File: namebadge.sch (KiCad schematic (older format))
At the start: 2 parts, among them U1 Pico

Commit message: power cap
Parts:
- added C15: 1000uF, Capacitor_THT:C_Radial_D12.5mm_H20.0mm_P5.00mm, symbol Device:C
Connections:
- net labels removed: Neo_DIN
- wire segments 22 -> 28
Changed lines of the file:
@@
 	1    0    0    -1
 $EndComp
-$Sheet
-S 6300 1400 1600 2250
-U 603C79C5
-F0 "letter-k" 50
-F1 "letter-k.sch" 50
-$EndSheet
-Text GLabel 4200 3550 2    50   Input ~ 0
-Neo_DIN
 Wire Wire Line
 	3250 1150 3250 1850
@@
 	2800 3550 3600 3550
 Wire Wire Line
-	3900 3550 4200 3550
+	5850 1050 5850 1150
+$Comp
+L Device:C C15
+U 1 1 6068DE58
+P 6000 1850
+F 0 "C15" V 5748 1850 50  0000 C CNN
+F 1 "1000uF" V 5839 1850 50  0000 C CNN
+F 2 "Capacitor_THT:C_Radial_D12.5mm_H20.0mm_P5.00mm" H 6038 1700 50  0001 C CNN
+F 3 "~" H 6000 1850 50  0001 C CNN
+	1    6000 1850
+	0    1    1    0
+$EndComp
+$Comp
+L power:GND #PWR0111
+U 1 1 6068F796
+P 6150 1950
+F 0 "#PWR0111" H 6150 1700 50  0001 C CNN
+F 1 "GND" H 6155 1777 50  0000 C CNN
+F 2 "" H 6150 1950 50  0001 C CNN
+F 3 "" H 6150 1950 50  0001 C CNN
+	1    6150 1950
+	1    0    0    -1
+$EndComp
+Wire Wire Line
+	6150 1950 6150 1850
+$Comp
+L power:VCC #PWR0119
+U 1 1 6068FE64
+P 5850 1150
+F 0 "#PWR0119" H 5850 1000 50  0001 C CNN
+F 1 "VCC" H 5865 1323 50  0000 C CNN
+F 2 "" H 5850 1150 50  0001 C CNN
+F 3 "" H 5850 1150 50  0001 C CNN
+	1    5850 1150
+	1    0    0    -1
+$EndComp
+Wire Wire Line
+	5850 1150 5850 1850
+Connection ~ 5850 1150
+$Sheet
+S 6300 1500 1600 2250
+U 603C79C5
+F0 "letter-k" 50
+F1 "letter-k.sch" 50
+F2 "LED_PWR" I L 6300 2300 50
+F3 "LED_DIN" I L 6300 3550 50
+$EndSheet
+Wire Wire Line
+	5900 1850 5850 1850
+Connection ~ 5850 1850
+Wire Wire Line
+	5850 1850 5850 2300
+Wire Wire Line
+	5850 2300 6300 2300
+Wire Wire Line
+	3900 3550 6300 3550
 $EndSCHEMATC

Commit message: level shifter
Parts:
- added IC1: SN74AHCT125N, Package_DIP:DIP-14_W7.62mm, symbol Mouser:SN74AHCT125N
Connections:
- wire segments 28 -> 41
- no-connect marks 33 -> 42
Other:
- moved on the sheet: R1
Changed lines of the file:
@@
 L Device:R R1
 U 1 1 606620B5
-P 3750 3550
-F 0 "R1" V 3543 3550 50  0000 C CNN
-F 1 "500" V 3634 3550 50  0000 C CNN
-F 2 "Resistor_THT:R_Axial_DIN0207_L6.3mm_D2.5mm_P15.24mm_Horizontal" V 3680 3550 50  0001 C CNN
-F 3 "~" H 3750 3550 50  0001 C CNN
-	1    3750 3550
-	0    1    1    0
+P 5750 3200
+F 0 "R1" V 5543 3200 50  0000 C CNN
+F 1 "500" V 5634 3200 50  0000 C CNN
+F 2 "Resistor_THT:R_Axial_DIN0207_L6.3mm_D2.5mm_P15.24mm_Horizontal" V 5680 3200 50  0001 C CNN
+F 3 "~" H 5750 3200 50  0001 C CNN
+	1    5750 3200
+	-1   0    0    1
 $EndComp
-Wire Wire Line
-	2800 3550 3600 3550
 Wire Wire Line
 	5850 1050 5850 1150
@@
 Wire Wire Line
 	5850 2300 6300 2300
+$Comp
+L Mouser:SN74AHCT125N IC1
+U 1 1 60732053
+P 4300 2450
+F 0 "IC1" H 4850 2715 50  0000 C CNN
+F 1 "SN74AHCT125N" H 4850 2624 50  0000 C CNN
+F 2 "Package_DIP:DIP-14_W7.62mm" H 5250 2550 50  0001 L CNN
+F 3 "http://www.ti.com/lit/gpn/sn74ahct125" H 5250 2450 50  0001 L CNN
+F 4 "Quadruple Bus Buffer Gates With 3-State Outputs" H 5250 2350 50  0001 L CNN "Description"
+F 5 "5.08" H 5250 2250 50  0001 L CNN "Height"
+F 6 "Texas Instruments" H 5250 2150 50  0001 L CNN "Manufacturer_Name"
+F 7 "SN74AHCT125N" H 5250 2050 50  0001 L CNN "Manufacturer_Part_Number"
+F 8 "595-SN74AHCT125N" H 5250 1950 50  0001 L CNN "Mouser Part Number"
+F 9 "https://www.mouser.co.uk/ProductDetail/Texas-Instruments/SN74AHCT125N?qs=1wQRf3HkBjyxwrHMwAiMfw%3D%3D" H 5250 1850 50  0001 L CNN "Mouser Price/Stock"
+F 10 "SN74AHCT125N" H 5250 1750 50  0001 L CNN "Arrow Part Number"
+F 11 "https://www.arrow.com/en/products/sn74ahct125n/texas-instruments" H 5250 1650 50  0001 L CNN "Arrow Price/Stock"
+	1    4300 2450
+	1    0    0    -1
+$EndComp
+NoConn ~ 4300 2750
+NoConn ~ 4300 2850
+NoConn ~ 4300 2950
+NoConn ~ 5400 3050
+NoConn ~ 5400 2950
+NoConn ~ 5400 2850
 Wire Wire Line
-	3900 3550 6300 3550
+	4200 3050 4300 3050
+$Comp
+L power:GND #PWR01
+U 1 1 6073F12A
+P 4850 3300
+F 0 "#PWR01" H 4850 3050 50  0001 C CNN
+F 1 "GND" H 4855 3127 50  0000 C CNN
+F 2 "" H 4850 3300 50  0001 C CNN
+F 3 "" H 4850 3300 50  0001 C CNN
+	1    4850 3300
+	1    0    0    -1
+$EndComp
+Wire Wire Line
+	5400 2450 5400 2300
+Wire Wire Line
+	5400 2300 5850 2300
+Connection ~ 5850 2300
+Wire Wire Line
+	5650 3550 5650 2650
+Wire Wire Line
+	5650 2650 5400 2650
+Wire Wire Line
+	2800 3550 5650 3550
+Wire Wire Line
+	5750 3350 5750 3550
+Wire Wire Line
+	5750 3550 6300 3550
+Wire Wire Line
+	4200 3050 4200 3300
+Connection ~ 4850 3300
+Wire Wire Line
+	4850 3300 4200 3300
+Wire Wire Line
+	4850 3300 5500 3300
+Wire Wire Line
+	5400 2750 5750 2750
+Wire Wire Line
+	5750 2750 5750 3050
+Wire Wire Line
+	5400 2550 5500 2550
+Wire Wire Line
+	5500 2550 5500 3300
+NoConn ~ 4300 2650
+NoConn ~ 4300 2550
+NoConn ~ 4300 2450
 $EndSCHEMATC

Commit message: DC jack take 1
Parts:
- added J1: Barrel_Jack, Connector_BarrelJack:BarrelJack_CUI_PJ-063AH_Horizontal, symbol Connector:Barrel_Jack
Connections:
- wire segments 41 -> 45
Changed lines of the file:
@@
 L power:VCC #PWR0126
 U 1 1 6054CB49
-P 1000 7150
-F 0 "#PWR0126" H 1000 7000 50  0001 C CNN
-F 1 "VCC" H 1015 7323 50  0000 C CNN
-F 2 "" H 1000 7150 50  0001 C CNN
-F 3 "" H 1000 7150 50  0001 C CNN
-	1    1000 7150
+P 1000 7400
+F 0 "#PWR0126" H 1000 7250 50  0001 C CNN
+F 1 "VCC" H 1015 7573 50  0000 C CNN
+F 2 "" H 1000 7400 50  0001 C CNN
+F 3 "" H 1000 7400 50  0001 C CNN
+	1    1000 7400
 	-1   0    0    1
 $EndComp
-Wire Wire Line
-	1000 7150 1000 7000
 $Comp
 L power:PWR_FLAG #FLG0102
@@
 L power:GND #PWR0127
 U 1 1 60577C01
-P 1450 7150
-F 0 "#PWR0127" H 1450 6900 50  0001 C CNN
-F 1 "GND" H 1455 6977 50  0000 C CNN
-F 2 "" H 1450 7150 50  0001 C CNN
-F 3 "" H 1450 7150 50  0001 C CNN
-	1    1450 7150
+P 1450 7400
+F 0 "#PWR0127" H 1450 7150 50  0001 C CNN
+F 1 "GND" H 1455 7227 50  0000 C CNN
+F 2 "" H 1450 7400 50  0001 C CNN
+F 3 "" H 1450 7400 50  0001 C CNN
+	1    1450 7400
 	1    0    0    -1
 $EndComp
-Wire Wire Line
-	1450 7150 1450 7000
 $Comp
 L Device:R R1
@@
 NoConn ~ 4300 2550
 NoConn ~ 4300 2450
+$Comp
+L Connector:Barrel_Jack J1
+U 1 1 6074B59D
+P 2050 7200
+F 0 "J1" H 1820 7158 50  0000 R CNN
+F 1 "Barrel_Jack" H 1820 7249 50  0000 R CNN
+F 2 "Connector_BarrelJack:BarrelJack_CUI_PJ-063AH_Horizontal" H 2100 7160 50  0001 C CNN
+F 3 "~" H 2100 7160 50  0001 C CNN
+	1    2050 7200
+	-1   0    0    1
+$EndComp
+Wire Wire Line
+	1450 7000 1450 7100
+Wire Wire Line
+	1000 7000 1000 7300
+Wire Wire Line
+	1750 7300 1000 7300
+Connection ~ 1000 7300
+Wire Wire Line
+	1000 7300 1000 7400
+Wire Wire Line
+	1750 7100 1450 7100
+Connection ~ 1450 7100
+Wire Wire Line
+	1450 7100 1450 7400
 $EndSCHEMATC

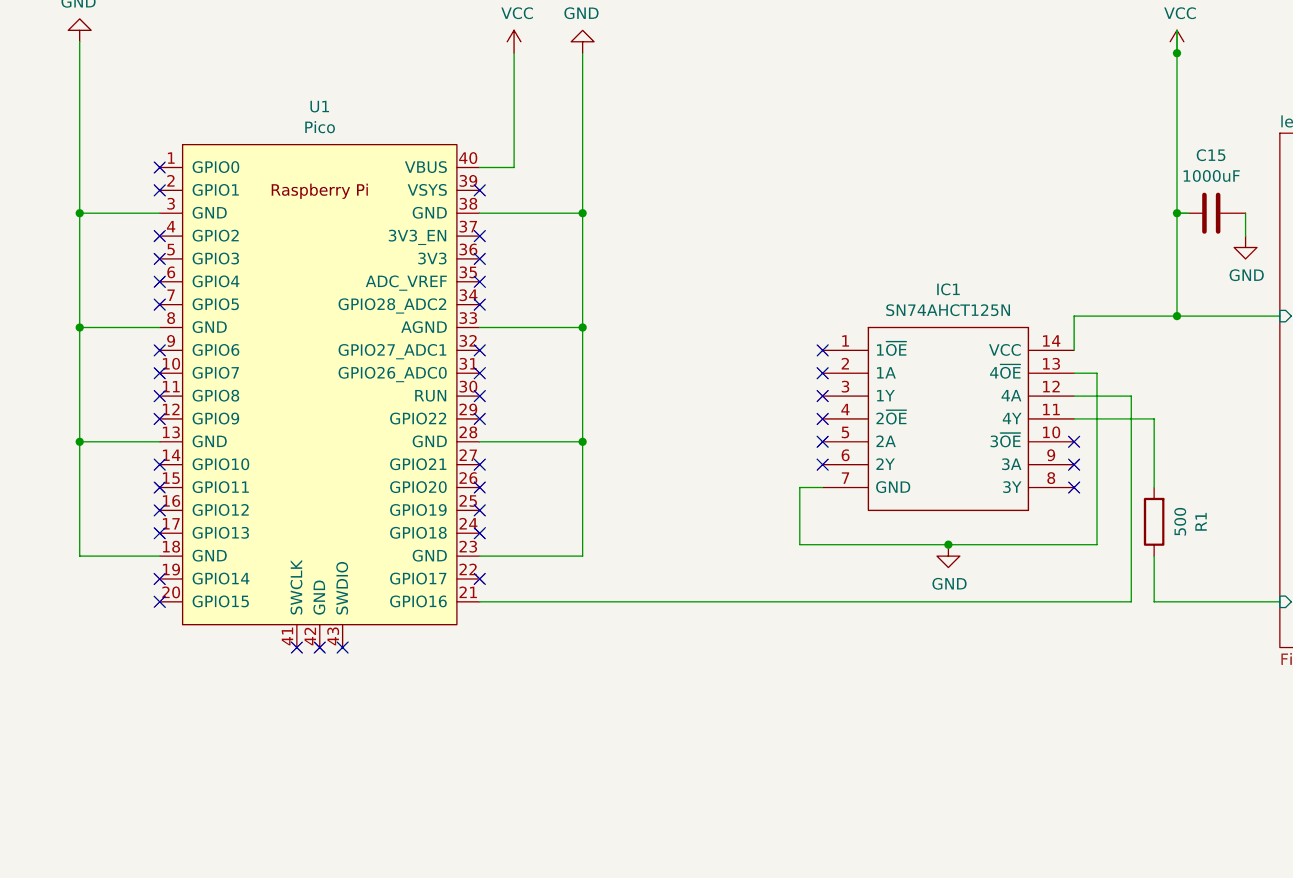
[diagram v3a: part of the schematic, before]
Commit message: fix traces after flip
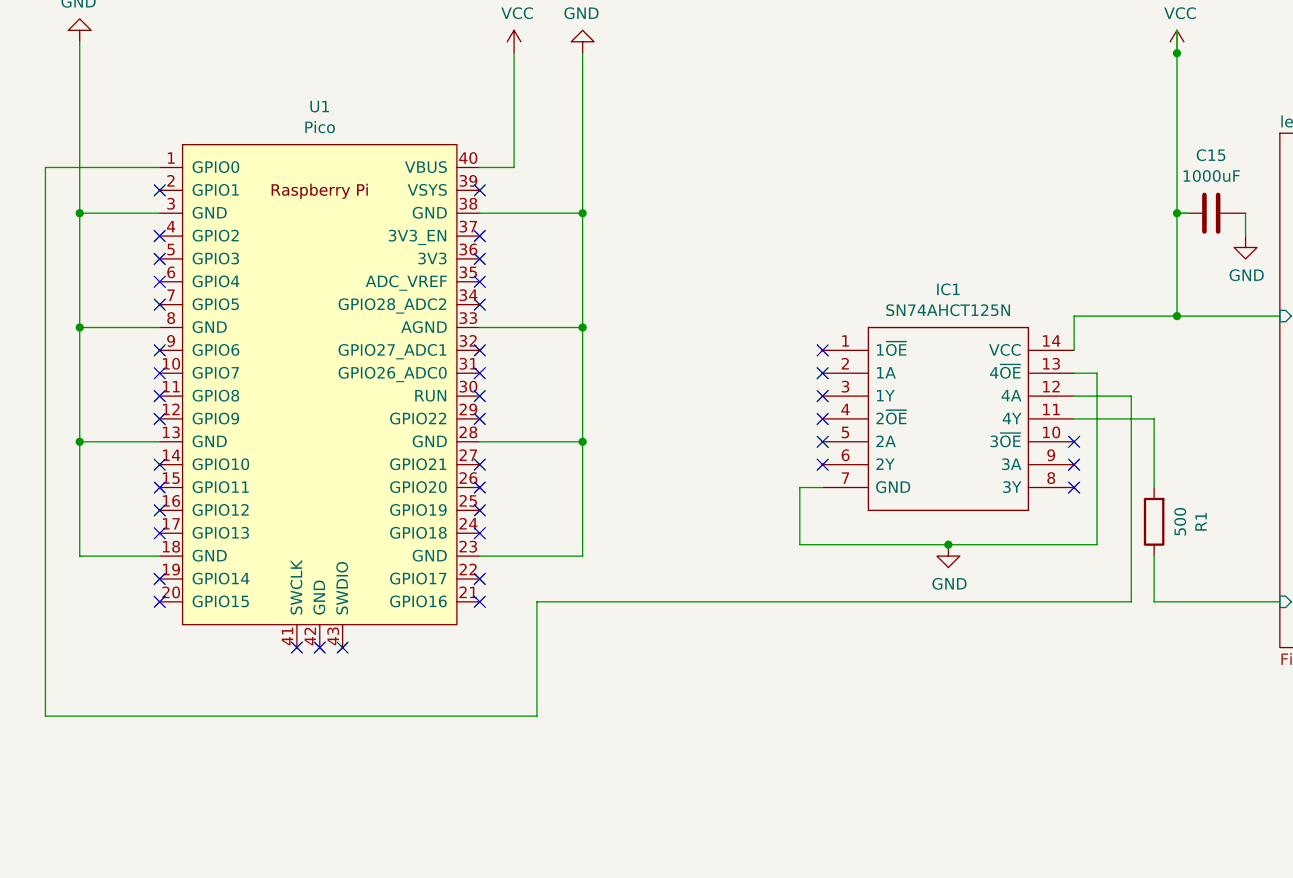
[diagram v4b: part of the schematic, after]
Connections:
- wire segments 45 -> 49
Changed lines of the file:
@@
 NoConn ~ 1400 1950
 NoConn ~ 1400 1750
-NoConn ~ 1400 1650
 NoConn ~ 2000 3750
 NoConn ~ 2100 3750
@@
 	5650 2650 5400 2650
 Wire Wire Line
-	2800 3550 5650 3550
-Wire Wire Line
 	5750 3350 5750 3550
 Wire Wire Line
@@
 Wire Wire Line
 	1450 7100 1450 7400
+Wire Wire Line
+	1400 1650 900  1650
+Wire Wire Line
+	900  1650 900  4050
+Wire Wire Line
+	900  4050 3050 4050
+Wire Wire Line
+	3050 4050 3050 3550
+Wire Wire Line
+	3050 3550 5650 3550
+NoConn ~ 2800 3550
 $EndSCHEMATC

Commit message: decoup for level shifter, layout cleanup
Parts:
- added C16: 0.1uF, Capacitor_THT:CP_Radial_D4.0mm_P2.00mm, symbol Device:CP_Small
- C15: footprint Capacitor_THT:C_Radial_D12.5mm_H20.0mm_P5.00mm -> Capacitor_THT:CP_Radial_D12.5mm_P5.00mm; symbol Device:C -> Device:CP
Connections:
- wire segments 49 -> 51
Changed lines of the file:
@@
 	5850 1050 5850 1150
-$Comp
-L Device:C C15
-U 1 1 6068DE58
-P 6000 1850
-F 0 "C15" V 5748 1850 50  0000 C CNN
-F 1 "1000uF" V 5839 1850 50  0000 C CNN
-F 2 "Capacitor_THT:C_Radial_D12.5mm_H20.0mm_P5.00mm" H 6038 1700 50  0001 C CNN
-F 3 "~" H 6000 1850 50  0001 C CNN
-	1    6000 1850
-	0    1    1    0
-$EndComp
 $Comp
 L power:GND #PWR0111
@@
 	5400 2450 5400 2300
 Wire Wire Line
-	5400 2300 5850 2300
+	5400 2300 5500 2300
 Connection ~ 5850 2300
 Wire Wire Line
@@
 	3050 3550 5650 3550
 NoConn ~ 2800 3550
+$Comp
+L Device:CP_Small C16
+U 1 1 60764BC0
+P 5500 2400
+F 0 "C16" H 5588 2446 50  0000 L CNN
+F 1 "0.1uF" H 5588 2355 50  0000 L CNN
+F 2 "Capacitor_THT:CP_Radial_D4.0mm_P2.00mm" H 5500 2400 50  0001 C CNN
+F 3 "~" H 5500 2400 50  0001 C CNN
+	1    5500 2400
+	1    0    0    -1
+$EndComp
+Connection ~ 5500 2300
+Wire Wire Line
+	5500 2300 5850 2300
+Wire Wire Line
+	5500 2500 5500 2550
+Connection ~ 5500 2550
+$Comp
+L Device:CP C15
+U 1 1 6068DE58
+P 6000 1850
+F 0 "C15" V 6255 1850 50  0000 C CNN
+F 1 "1000uF" V 6164 1850 50  0000 C CNN
+F 2 "Capacitor_THT:CP_Radial_D12.5mm_P5.00mm" H 6038 1700 50  0001 C CNN
+F 3 "~" H 6000 1850 50  0001 C CNN
+	1    6000 1850
+	0    -1   -1   0
+$EndComp
 $EndSCHEMATC

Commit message: switch
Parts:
- added SW1: SW_Push, Button_Switch_THT:SW_PUSH-12mm, symbol Switch:SW_Push
- R1: footprint Resistor_THT:R_Axial_DIN0207_L6.3mm_D2.5mm_P15.24mm_Horizontal -> Resistor_THT:R_Axial_DIN0207_L6.3mm_D2.5mm_P10.16mm_Horizontal
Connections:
- wire segments 51 -> 60
- no-connect marks 42 -> 41
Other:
- moved on the sheet: C16, R1
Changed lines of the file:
@@
 $EndComp
-Wire Wire Line
-	3250 1150 3250 1850
 Wire Wire Line
 	3250 3350 2800 3350
@@
 Wire Wire Line
 	2800 1850 3250 1850
-Connection ~ 3250 1850
 Wire Wire Line
 	3250 1850 3250 2350
 Wire Wire Line
-	2800 1650 2950 1650
-Wire Wire Line
-	2950 1650 2950 1150
+	2800 1650 4000 1650
+Wire Wire Line
+	4000 1650 4000 1550
 $Comp
 L power:VCC #PWR0101
 U 1 1 6053EF5E
-P 2950 1150
-F 0 "#PWR0101" H 2950 1000 50  0001 C CNN
-F 1 "VCC" H 2965 1323 50  0000 C CNN
-F 2 "" H 2950 1150 50  0001 C CNN
-F 3 "" H 2950 1150 50  0001 C CNN
-	1    2950 1150
-	1    0    0    -1
-$EndComp
-$Comp
-L power:GND #PWR0102
-U 1 1 6053F8EA
-P 3250 1150
-F 0 "#PWR0102" H 3250 900 50  0001 C CNN
-F 1 "GND" H 3255 977 50  0000 C CNN
-F 2 "" H 3250 1150 50  0001 C CNN
-F 3 "" H 3250 1150 50  0001 C CNN
-	1    3250 1150
-	-1   0    0    1
+P 4000 1550
+F 0 "#PWR0101" H 4000 1400 50  0001 C CNN
+F 1 "VCC" H 4015 1723 50  0000 C CNN
+F 2 "" H 4000 1550 50  0001 C CNN
+F 3 "" H 4000 1550 50  0001 C CNN
+	1    4000 1550
+	1    0    0    -1
 $EndComp
 Wire Wire Line
 	1400 1850 1050 1850
 Wire Wire Line
-	1050 1850 1050 1100
+	1050 1850 1050 1250
 Wire Wire Line
 	1050 1850 1050 2350
@@
 	-1   0    0    1
 $EndComp
-NoConn ~ 2800 1750
 NoConn ~ 2800 1950
 NoConn ~ 2800 2050
@@
 NoConn ~ 2800 3250
 NoConn ~ 2800 3450
-NoConn ~ 1400 3550
 NoConn ~ 1400 3450
 NoConn ~ 1400 3250
@@
 L Device:R R1
 U 1 1 606620B5
-P 5750 3200
-F 0 "R1" V 5543 3200 50  0000 C CNN
-F 1 "500" V 5634 3200 50  0000 C CNN
-F 2 "Resistor_THT:R_Axial_DIN0207_L6.3mm_D2.5mm_P15.24mm_Horizontal" V 5680 3200 50  0001 C CNN
-F 3 "~" H 5750 3200 50  0001 C CNN
-	1    5750 3200
-	-1   0    0    1
-$EndComp
-Wire Wire Line
-	5850 1050 5850 1150
+P 5900 3550
+F 0 "R1" V 5693 3550 50  0000 C CNN
+F 1 "500" V 5784 3550 50  0000 C CNN
+F 2 "Resistor_THT:R_Axial_DIN0207_L6.3mm_D2.5mm_P10.16mm_Horizontal" V 5830 3550 50  0001 C CNN
+F 3 "~" H 5900 3550 50  0001 C CNN
+	1    5900 3550
+	0    1    -1   0
+$EndComp
 $Comp
 L power:GND #PWR0111
@@
 Wire Wire Line
 	6150 1950 6150 1850
-$Comp
-L power:VCC #PWR0119
-U 1 1 6068FE64
-P 5850 1150
-F 0 "#PWR0119" H 5850 1000 50  0001 C CNN
-F 1 "VCC" H 5865 1323 50  0000 C CNN
-F 2 "" H 5850 1150 50  0001 C CNN
-F 3 "" H 5850 1150 50  0001 C CNN
-	1    5850 1150
-	1    0    0    -1
-$EndComp
-Wire Wire Line
-	5850 1150 5850 1850
-Connection ~ 5850 1150
 $Sheet
 S 6300 1500 1600 2250
@@
 NoConn ~ 5400 2950
 NoConn ~ 5400 2850
-Wire Wire Line
-	4200 3050 4300 3050
 $Comp
 L power:GND #PWR01
 U 1 1 6073F12A
-P 4850 3300
-F 0 "#PWR01" H 4850 3050 50  0001 C CNN
-F 1 "GND" H 4855 3127 50  0000 C CNN
-F 2 "" H 4850 3300 50  0001 C CNN
-F 3 "" H 4850 3300 50  0001 C CNN
-	1    4850 3300
-	1    0    0    -1
-$EndComp
-Wire Wire Line
-	5400 2450 5400 2300
-Wire Wire Line
-	5400 2300 5500 2300
-Connection ~ 5850 2300
-Wire Wire Line
-	5650 3550 5650 2650
-Wire Wire Line
-	5650 2650 5400 2650
-Wire Wire Line
-	5750 3350 5750 3550
-Wire Wire Line
-	5750 3550 6300 3550
-Wire Wire Line
-	4200 3050 4200 3300
-Connection ~ 4850 3300
-Wire Wire Line
-	4850 3300 4200 3300
-Wire Wire Line
-	4850 3300 5500 3300
-Wire Wire Line
-	5400 2750 5750 2750
-Wire Wire Line
-	5750 2750 5750 3050
-Wire Wire Line
-	5400 2550 5500 2550
-Wire Wire Line
-	5500 2550 5500 3300
+P 4200 3450
+F 0 "#PWR01" H 4200 3200 50  0001 C CNN
+F 1 "GND" H 4205 3277 50  0000 C CNN
+F 2 "" H 4200 3450 50  0001 C CNN
+F 3 "" H 4200 3450 50  0001 C CNN
+	1    4200 3450
+	1    0    0    -1
+$EndComp
+Wire Wire Line
+	5700 1250 5700 2650
+Wire Wire Line
+	5700 2650 5400 2650
+Wire Wire Line
+	5400 2750 5700 2750
+Wire Wire Line
+	5400 2550 5550 2550
 NoConn ~ 4300 2650
 NoConn ~ 4300 2550
@@
 	1450 7100 1450 7400
 Wire Wire Line
-	1400 1650 900  1650
-Wire Wire Line
-	900  1650 900  4050
-Wire Wire Line
-	900  4050 3050 4050
-Wire Wire Line
-	3050 4050 3050 3550
-Wire Wire Line
-	3050 3550 5650 3550
-NoConn ~ 2800 3550
-$Comp
-L Device:CP_Small C16
-U 1 1 60764BC0
-P 5500 2400
-F 0 "C16" H 5588 2446 50  0000 L CNN
-F 1 "0.1uF" H 5588 2355 50  0000 L CNN
-F 2 "Capacitor_THT:CP_Radial_D4.0mm_P2.00mm" H 5500 2400 50  0001 C CNN
-F 3 "~" H 5500 2400 50  0001 C CNN
-	1    5500 2400
-	1    0    0    -1
-$EndComp
-Connection ~ 5500 2300
-Wire Wire Line
-	5500 2300 5850 2300
-Wire Wire Line
-	5500 2500 5500 2550
-Connection ~ 5500 2550
+	1400 1650 1200 1650
+Wire Wire Line
+	1200 1650 1200 1250
 $Comp
 L Device:CP C15
@@
 	0    -1   -1   0
 $EndComp
+$Comp
+L Switch:SW_Push SW1
+U 1 1 6078F24C
+P 1500 4250
+F 0 "SW1" H 1500 4065 50  0000 C CNN
+F 1 "SW_Push" H 1500 4156 50  0000 C CNN
+F 2 "Button_Switch_THT:SW_PUSH-12mm" H 1500 4450 50  0001 C CNN
+F 3 "~" H 1500 4450 50  0001 C CNN
+	1    1500 4250
+	-1   0    0    1
+$EndComp
+Wire Wire Line
+	1200 1250 3250 1250
+NoConn ~ 2800 3550
+$Comp
+L Device:CP_Small C16
+U 1 1 60764BC0
+P 4000 3050
+F 0 "C16" V 4225 3050 50  0000 C CNN
+F 1 "0.1uF" V 4134 3050 50  0000 C CNN
+F 2 "Capacitor_THT:CP_Radial_D4.0mm_P2.00mm" H 4000 3050 50  0001 C CNN
+F 3 "~" H 4000 3050 50  0001 C CNN
+	1    4000 3050
+	0    -1   -1   0
+$EndComp
+Wire Wire Line
+	4300 3050 4200 3050
+Wire Wire Line
+	4200 3050 4200 3300
+Connection ~ 4200 3050
+Wire Wire Line
+	4200 3050 4100 3050
+Wire Wire Line
+	3850 3050 3850 2050
+Wire Wire Line
+	3850 2050 4800 2050
+Wire Wire Line
+	5400 2050 5400 2450
+Wire Wire Line
+	5550 2550 5550 3300
+Wire Wire Line
+	4200 3300 5550 3300
+Connection ~ 4200 3300
+Wire Wire Line
+	4200 3300 4200 3450
+Wire Wire Line
+	3850 3050 3900 3050
+Wire Wire Line
+	5700 3550 5750 3550
+Wire Wire Line
+	5700 2750 5700 3550
+Wire Wire Line
+	6300 3550 6050 3550
+Wire Wire Line
+	1200 3550 1200 4250
+Wire Wire Line
+	1200 4250 1300 4250
+Wire Wire Line
+	1200 3550 1400 3550
+$Comp
+L power:GND #PWR0120
+U 1 1 607D0FE8
+P 1850 4300
+F 0 "#PWR0120" H 1850 4050 50  0001 C CNN
+F 1 "GND" H 1855 4127 50  0000 C CNN
+F 2 "" H 1850 4300 50  0001 C CNN
+F 3 "" H 1850 4300 50  0001 C CNN
+	1    1850 4300
+	1    0    0    -1
+$EndComp
+Wire Wire Line
+	1700 4250 1850 4250
+Wire Wire Line
+	1850 4250 1850 4300
+NoConn ~ 2800 1750
+Wire Wire Line
+	4000 1650 4800 1650
+Wire Wire Line
+	4800 1650 4800 2050
+Connection ~ 4000 1650
+Connection ~ 4800 2050
+Wire Wire Line
+	4800 2050 5400 2050
+Wire Wire Line
+	1200 1250 1050 1250
+Connection ~ 1200 1250
+Connection ~ 1050 1250
+Wire Wire Line
+	1050 1250 1050 1100
+Wire Wire Line
+	5850 1500 5850 1850
+$Comp
+L power:VCC #PWR0119
+U 1 1 6068FE64
+P 5850 1500
+F 0 "#PWR0119" H 5850 1350 50  0001 C CNN
+F 1 "VCC" H 5865 1673 50  0000 C CNN
+F 2 "" H 5850 1500 50  0001 C CNN
+F 3 "" H 5850 1500 50  0001 C CNN
+	1    5850 1500
+	1    0    0    -1
+$EndComp
+Wire Wire Line
+	3250 1850 3250 1250
+Connection ~ 3250 1850
+Connection ~ 3250 1250
+Wire Wire Line
+	3250 1250 5700 1250
 $EndSCHEMATC
